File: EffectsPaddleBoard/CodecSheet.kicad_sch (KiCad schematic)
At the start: 22 parts, among them U3 TLV320AIC3100

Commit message: Corrections, see comments
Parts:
- removed C20: 1m, Capacitor_SMD:C_1206_3216Metric, symbol Device:C
- removed R19, R20: 10k, Resistor_SMD:R_0402_1005Metric, symbol Device:R
- added C50: 47u, Capacitor_SMD:C_1206_3216Metric, symbol Device:C_Small
- added J5, J6: AudioJack2, Connector_Audio:Jack_6.35mm_Neutrik_NJ2FD-V_Vertical, symbol Connector_Audio:AudioJack2
- added R23: 10k, Resistor_SMD:R_0402_1005Metric, symbol Device:R
- C19: value 1m -> 1u; footprint Capacitor_SMD:C_1206_3216Metric -> Capacitor_SMD:C_1210_3225Metric
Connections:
- net Analog_In_R: now also R23.1
- net GND: now also J5.S, J6.S, R23.2
- net HPL: now also C50.1
- net Analog_In1: no longer names the net of C19.2
- net Analog_In1: now also J5.T
- net Audio_M: no longer names the net of U3.19 (SPKM), U3.23 (SPKM)
- net Audio_P: no longer names the net of U3.22 (SPKP), U3.26 (SPKP)
- net HPR: no longer names the net of U3.30 (HPR)
- new net AudioOutBoard: C50.2, J6.T
- no-connect marks 0 -> 3
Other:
- note added: "Decrease caps in 3 orders of magnitude"
- note added: "Footprints to 0805"
- note added: "Research volume control"

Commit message: Corrected the board, now all parts should be right
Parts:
- added C30: 1u, Capacitor_SMD:C_0805_2012Metric, symbol Device:C
- added R5: 0, Resistor_SMD:R_0402_1005Metric, symbol Device:R
- C11, C13, C15, C17, C33, C35: value 100u -> 100n; footprint Capacitor_SMD:C_1206_3216Metric -> Capacitor_SMD:C_0402_1005Metric
- C12, C14: value 22m -> 22u; footprint Capacitor_SMD:C_1206_3216Metric -> Capacitor_SMD:C_0805_2012Metric
- C16, C18, C34, C36: value 10m -> 10u; footprint Capacitor_SMD:C_1206_3216Metric -> Capacitor_SMD:C_0805_2012Metric
- C19: footprint Capacitor_SMD:C_1210_3225Metric -> Capacitor_SMD:C_0805_2012Metric
- C50: footprint Capacitor_SMD:C_1206_3216Metric -> Capacitor_SMD:C_0805_2012Metric
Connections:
- net Analog_In_R: now also C30.1
- net at C19.2, J5.T: now also R5.1
- new net: C30.2, R5.2
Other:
- note removed: "Decrease caps in 3 orders of magnitude"
- note removed: "Footprints to 0805"

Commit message: Layout completed
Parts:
- added C31: 47u, Capacitor_SMD:C_0805_2012Metric, symbol Device:C
- added R6: 0, Resistor_SMD:R_0402_1005Metric, symbol Device:R
- added RV1: 10k, Potentiometer_THT:Potentiometer_ACP_CA9-H2,5_Horizontal, symbol Device:R_Potentiometer_Small
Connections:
- net +3.3VA: now also R18.1
- net AudioOutBoard: now also C31.2
- net GND: now also RV1.3; no longer R18.2
- net Volume: now also RV1.2; no longer R18.1
- net at U3.30 (HPR): now also R6.1
- new net: C31.1, R6.2
- new net VolumeVDiv: R18.2, RV1.1
- no-connect marks 3 -> 2
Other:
- note removed: "Research volume control"
- moved on the sheet: R18

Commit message: Added all parts
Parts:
- C11, C13, C15, C17, C33, C35: Distributer Link https://www.mouser.ch/ProductDetail/Murata-Electronics/GRM3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 -> https://www.mouser.ch/ProductDetail/Murata-Electronics/GRM1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; Manufacturer Part Number GRM31CR61A107MEA8L -> GRM155R61C104KA88J
- C12, C14: Distributer Link (none) -> https://www.mouser.ch/ProductDetail/Murata-Electronics/GRM2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; Manufacturer (none) -> Murata Electronics; Manufacturer Part Number (none) -> GRM21BC81C226ME44L
- C16, C18, C34, C36: Distributer Link (none) -> https://www.mouser.ch/ProductDetail/Murata-Electronics/GCM2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; Manufacturer (none) -> Murata Electronics; Manufacturer Part Number (none) -> GCM21BC71E106KE36K
- C19, C30: Distributer Link (none) -> https://www.mouser.ch/ProductDetail/Murata-Electronics/GRM2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; Manufacturer (none) -> Murata Electronics; Manufacturer Part Number (none) -> GRM21BR71C105KA01K
- C31: Distributer Link (none) -> https://www.mouser.ch/ProductDetail/Murata-Electronics/GRM2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; Manufacturer (none) -> Murata Electronics; Manufacturer Part Number (none) -> GRM21BR61A476ME15K
- C50: Distributer Link https://www.mouser.ch/ProductDetail/Murata-Electronics/GRM3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 -> https://www.mouser.ch/ProductDetail/Murata-Electronics/GRM2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; Manufacturer Part Number GRM31CR71C106KAC7L -> GRM21BR61A476ME15K
- R16, R17, R18, R23: Distributer Link (none) -> https://www.mouser.ch/ProductDetail/Vishay-Beyschlag/MCS040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; Manufacturer (none) -> Vishay / Beyschlag; Manufacturer Part Number (none) -> MCS04020D1002BE000
- R3, R4: Distributer Link (none) -> https://www.mouser.ch/ProductDetail/Vishay-Beyschlag/MCS040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; Manufacturer (none) -> Vishay / Beyschlag; Manufacturer Part Number (none) -> MCS04020D2201BE000
- R5, R6: Distributer Link (none) -> https://www.mouser.ch/ProductDetail/Vishay-Beyschlag/MCS040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; Manufacturer (none) -> Vishay / Beyschlag; Manufacturer Part Number (none) -> MCS0402HZ0000ZE100

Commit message: exported symbols and footprints, updated PCB
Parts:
- C11, C12, C13, C14, C15, C16, C17, C18, C19, C30, C31, C33, C34, C35, C36: symbol Device:C -> EffectsPaddleBoard:C
- C50: symbol Device:C_Small -> EffectsPaddleBoard:C_Small
- J5, J6: symbol Connector_Audio:AudioJack2 -> EffectsPaddleBoard:AudioJack2
- R16, R17, R18, R23, R3, R4, R5, R6: symbol Device:R -> EffectsPaddleBoard:R
- RV1: symbol Device:R_Potentiometer_Small -> EffectsPaddleBoard:R_Potentiometer_Small
- U3: symbol Audio:TLV320AIC3100 -> EffectsPaddleBoard:TLV320AIC3100
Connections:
- net at U3.19 (SPKM): no longer U3.23 (SPKM)
- net at U3.22 (SPKP): no longer U3.26 (SPKP)
- no-connect marks 2 -> 4
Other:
- note added: "TODO: 20kHz low pass"
- note removed: "is termination needed?"
- moved on the sheet: C11, C12, C13, C14, C15, C16, C17, C18, C19, C31, C33, C34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

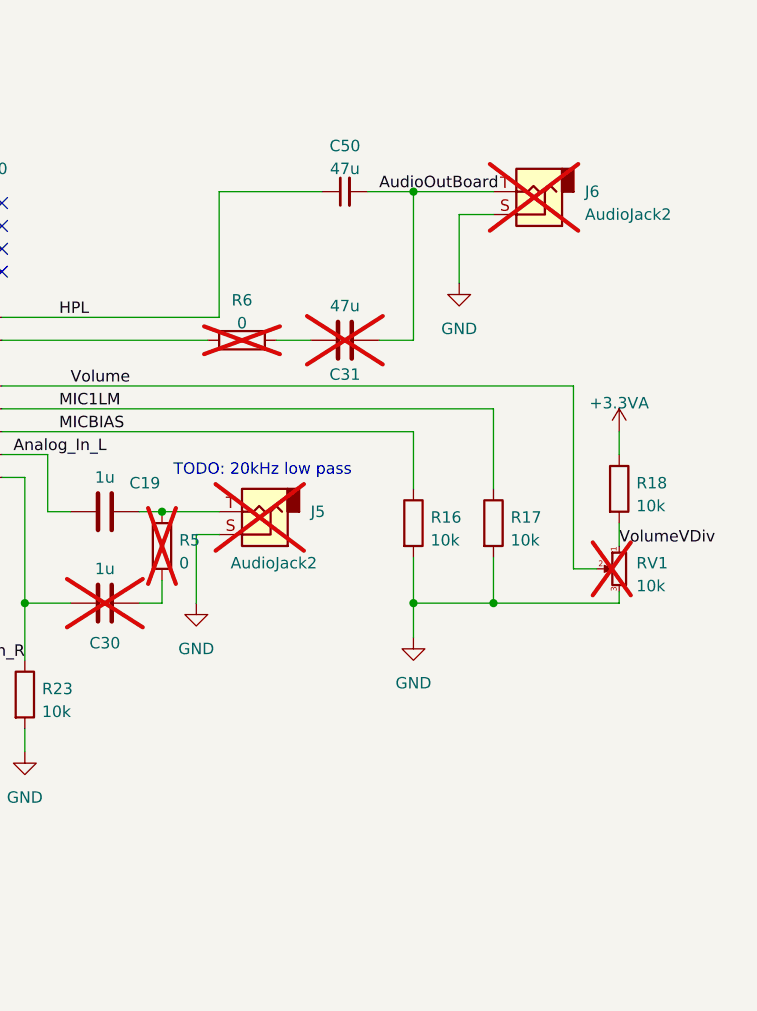
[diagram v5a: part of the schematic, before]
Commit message: Begun with double sided layout
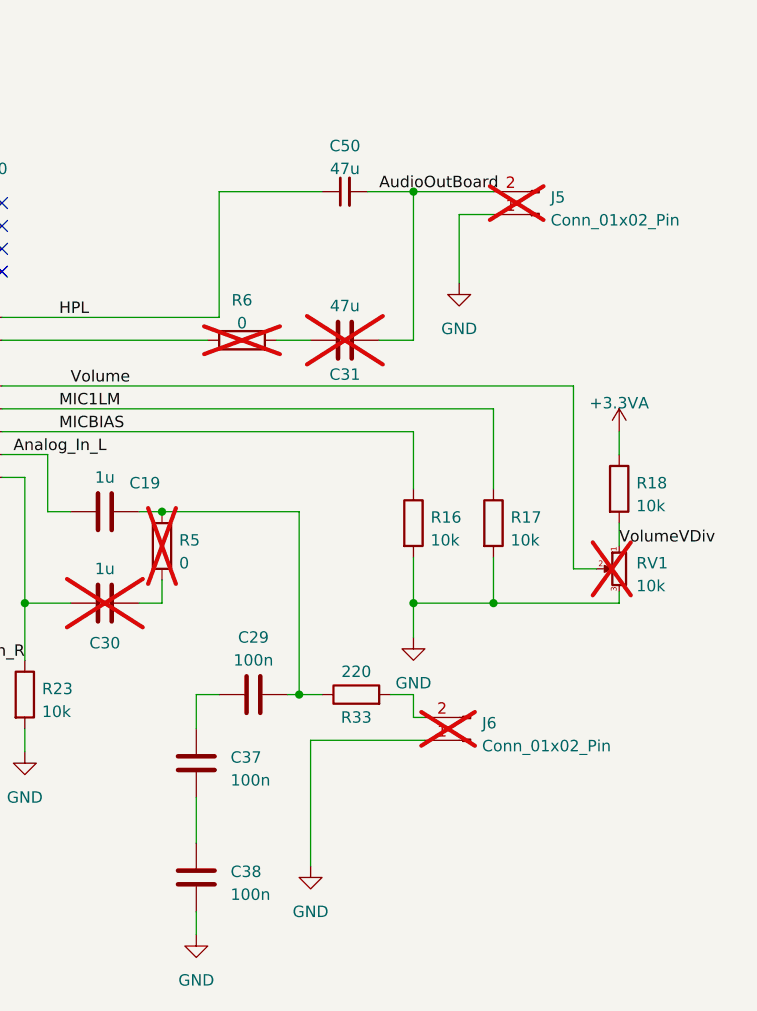
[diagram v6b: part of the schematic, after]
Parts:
- removed J5, J6: AudioJack2, Connector_Audio:Jack_6.35mm_Neutrik_NJ2FD-V_Vertical, symbol EffectsPaddleBoard:AudioJack2
- added C29, C37, C38: 100n, Capacitor_SMD:C_0402_1005Metric, symbol EffectsPaddleBoard:C
- added J5, J6: Conn_01x02_Pin, Connector_PinHeader_2.54mm:PinHeader_1x02_P2.54mm_Vertical, symbol Connector:Conn_01x02_Pin
- added R33: 220, Resistor_SMD:R_0402_1005Metric, symbol EffectsPaddleBoard:R
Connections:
- net AudioOutBoard: now also J5.2 (Pin_2)
- net GND: now also C38.1, J5.1 (Pin_1), J6.1 (Pin_1)
- net at C19.2, R5.1: now also C29.2, R33.1
- new net: J6.2 (Pin_2), R33.2
- new net: C29.1, C37.2
- new net: C37.1, C38.2
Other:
- note removed: "TODO: 20kHz low pass"

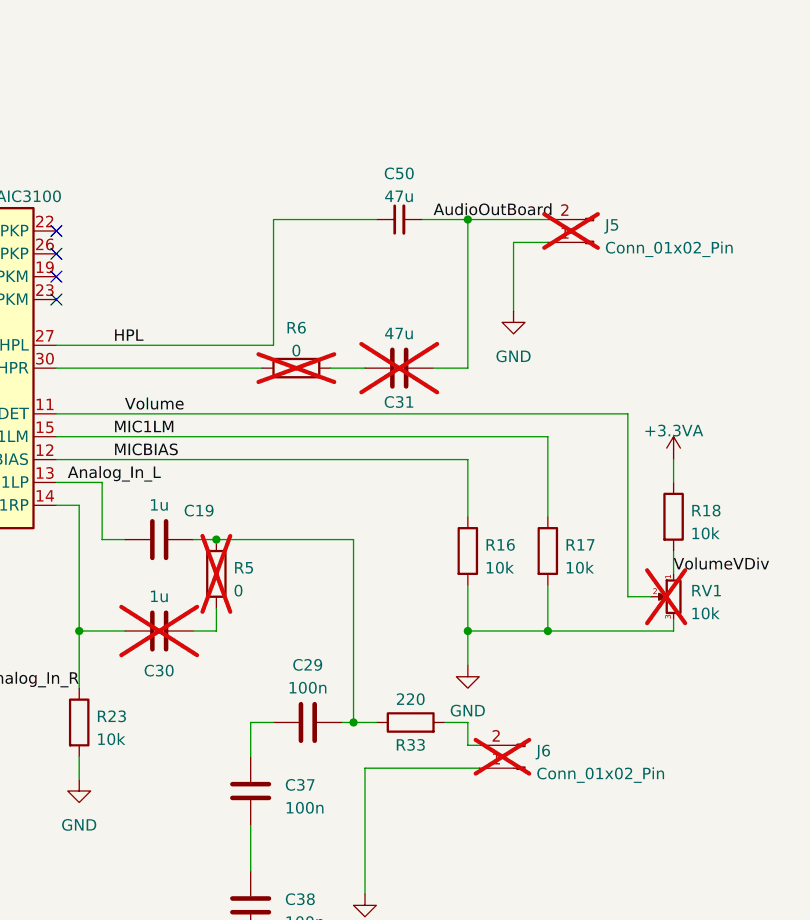
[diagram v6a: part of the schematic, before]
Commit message: Upgraded to kicad8 and improved layout
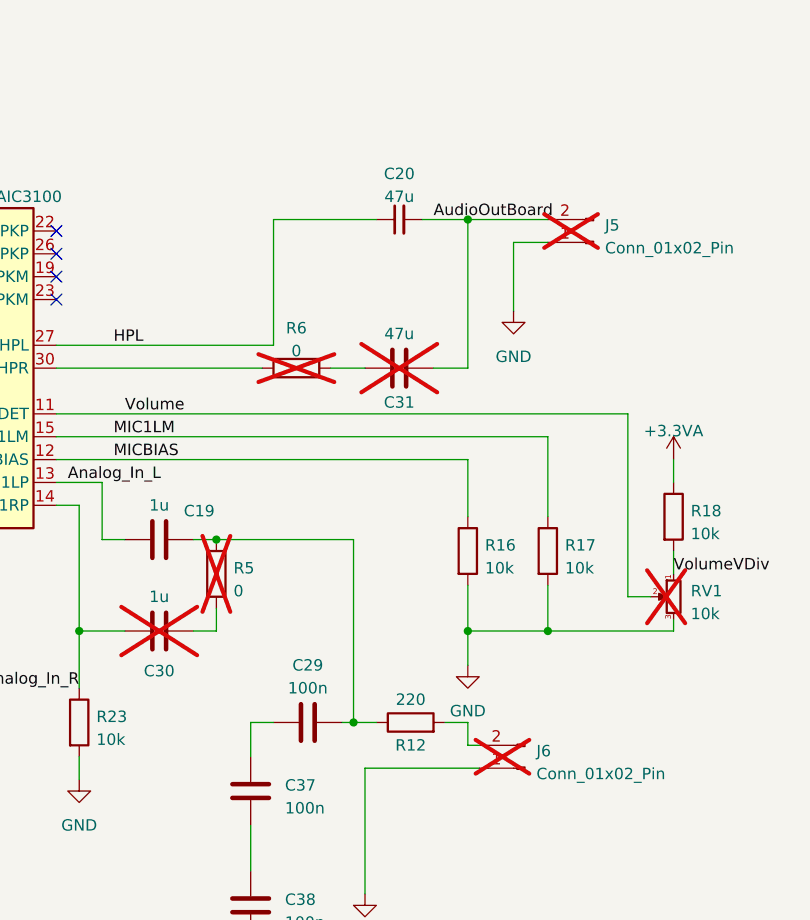
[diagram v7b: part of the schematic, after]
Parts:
- C11, C13, C15, C17, C29, C33, C35, C37, C38: footprint Capacitor_SMD:C_0402_1005Metric -> Capacitor_SMD:C_0603_1608Metric
- R12: renamed from R33; footprint Resistor_SMD:R_0402_1005Metric -> Resistor_SMD:R_0603_1608Metric
- R16, R17, R18, R23, R3, R4, R5, R6: footprint Resistor_SMD:R_0402_1005Metric -> Resistor_SMD:R_0603_1608Metric
- renumbered C50 to C20
